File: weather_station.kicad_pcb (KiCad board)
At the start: 2 copper layers, 100 x 140 mm, 78 parts, among them J3 Conn_Coaxial, Q1 Q_NMOS_DGS, U1 LT1129CS8-3.3, U2 ADS1120-PW, U3 nRF52832, U4 LP3947, U5 MPL115A1, U6 MPU-9250, Y1 FL3200037

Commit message: updates
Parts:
- removed D1: D_Zener, Diodes_SMD:D_0603
- added AE1: ant, Microwave:SMA, F.Cu at (93.7, 86.6)
- added C29: C_Small, Capacitors_SMD:C_0402, B.Cu at (61.2, 88.6)
- added C30: C_Small, Capacitors_SMD:C_0402, B.Cu at (61.2, 93.7)
- added J1: Conn_02x10_Odd_Even, Pin_Headers:Pin_Header_Straight_2x10_Pitch2.54mm, F.Cu at (119.0, 172.7)
- added J2: Conn_02x10_Odd_Even, Pin_Headers:Pin_Header_Straight_2x10_Pitch2.54mm, F.Cu at (115.6, 59.9)
- added J4: Conn_Coaxial, Connectors:SMA_SMD_Jack_Straight, B.Cu at (85.9, 76.4)
- added M1: ANEOMETER, Wire_Connections_Bridges:WireConnection_2.00mmDrill, B.Cu at (24.1, 94.5)
- added R21: R_Small, Resistors_SMD:R_0603, B.Cu at (36.6, 94.3)
- added Y2: 32.786khz, Crystals:Crystal_SMD_EuroQuartz_EQ161-2pin_3.2x1.5mm, B.Cu at (61.2, 91.2)
- JP1: moved to B.Cu
- moved C18 60.3 mm to (52.1, 103.1), turned to 270 degrees
- moved L4 18.5 mm to (88.1, 86.4), turned to 270 degrees
- moved D2 18.4 mm to (77.5, 74.4), turned to 270 degrees
- moved C13 16.6 mm to (89.7, 86.3), turned to 90 degrees
- moved C12 16.5 mm to (86.4, 86.1), turned to 270 degrees
- moved L3 15.1 mm to (82.5, 86.4), turned to 90 degrees
- moved R7 13.9 mm to (76.2, 78.5), turned to 90 degrees
- moved R8 13.0 mm to (77.5, 78.5), turned to 90 degrees
- moved R9 12.4 mm to (78.7, 78.5), turned to 90 degrees
- moved C11 12.0 mm to (81.3, 86.4), turned to 270 degrees
- moved C8 7.29 mm to (65.5, 96.1)
- moved C10 6.82 mm to (67.1, 96.0)
- moved C9 1.30 mm to (75.9, 90.7), turned to 0 degrees
- turned JP1 to 90 degrees
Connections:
- U3 pad 10: Net-(U3-Pad10) -> ANEOMETER
- U3 pad 16: RADIO_PTT -> RADIO_PD
- U3 pad 17: RADIO_DATA -> RADIO_PTT
- U3 pad 18: RADIO_UART_TX -> RADIO_DATA
- U3 pad 19: RADIO_UART_RX -> RADIO_UART_TX
- U3 pad 2: Net-(U3-Pad2) -> XL1
- U3 pad 20: Net-(U3-Pad20) -> RADIO_UART_RX
- U3 pad 3: Net-(U3-Pad3) -> XL2
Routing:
- net +3V3: track 150.7 -> 241.2 mm
- net SWDIO: track 0.00 -> 73.5 mm
- net RESET: track 0.00 -> 73.4 mm
- net SWO: track 0.00 -> 71.1 mm
- net RADIO_PD: track 0.00 -> 70.1 mm
- net SWCLK: track 0.00 -> 64.1 mm
- net ANEOMETER: track 0.00 -> 44.7 mm
- net Net-(C12-Pad2): track 0.00 -> 16.8 mm
- net Net-(M1-Pad1): track 0.00 -> 11.8 mm
- net Net-(C11-Pad1): track 0.00 -> 9.93 mm
- net Net-(C11-Pad2): track 0.00 -> 9.64 mm
- net GND: track 62.1 -> 71.4 mm, vias 16 -> 19
- net XL2: track 0.00 -> 7.89 mm
- net XL1: track 0.00 -> 7.55 mm
- net R_LED: track 18.8 -> 11.3 mm
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- added copper zone on F.Cu, net GND

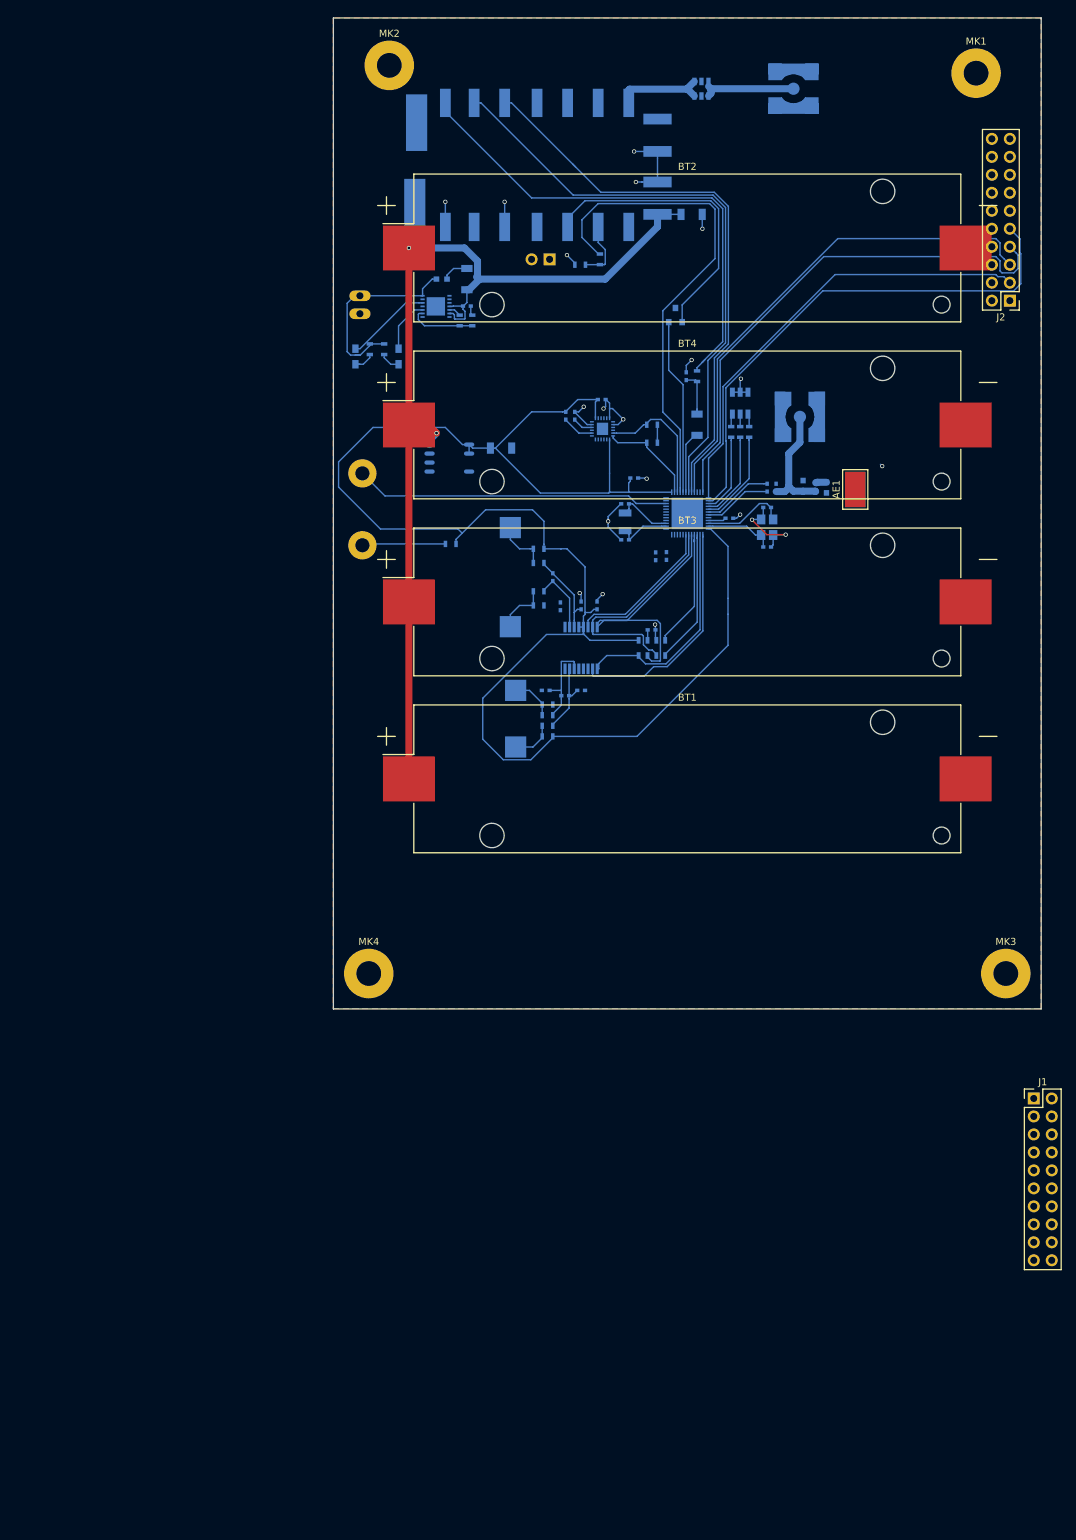
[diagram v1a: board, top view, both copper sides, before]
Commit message: basing solar power supply off of openMPPT
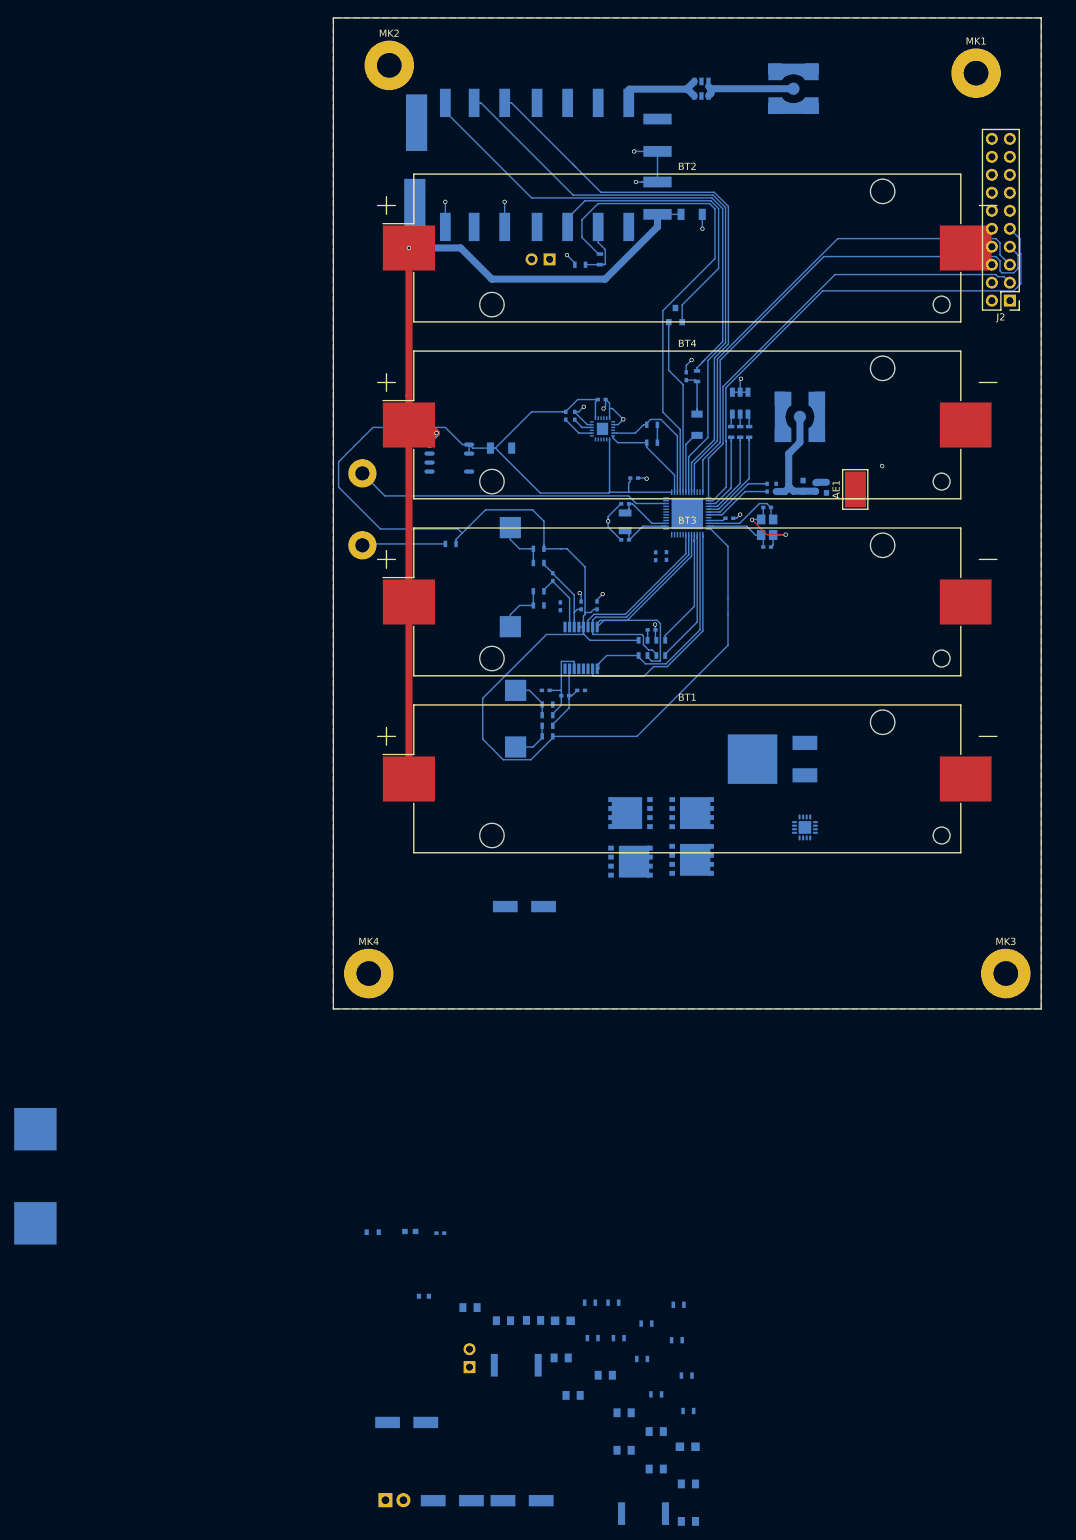
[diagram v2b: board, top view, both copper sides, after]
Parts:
- removed J1: Conn_02x10_Odd_Even, Pin_Headers:Pin_Header_Straight_2x10_Pitch2.54mm
- removed SC1: Solar_Cell, Connectors:PINHEAD1-2
- added C31: 0.1uF, Capacitors_SMD:C_0805, B.Cu at (65.6, 219.7)
- added C32: 1.0uF, Capacitors_SMD:C_0805, B.Cu at (65.6, 225.0)
- added C33: 0.1uF, Capacitors_SMD:C_0805, B.Cu at (70.2, 227.1)
- added C34: 1.0uF, Capacitors_SMD:C_0805, B.Cu at (61.1, 217.1)
- added C35: CP, Capacitors_SMD:CP_Elec_6.3x7.7, B.Cu at (30.4, 218.4)
- added C36: CP, Capacitors_SMD:CP_Elec_6.3x7.7, B.Cu at (47.0, 145.5)
- added C37: 1.0uF, Capacitors_SMD:C_0805, B.Cu at (70.2, 232.4)
- added C38: 0.1uF, Capacitors_SMD:C_0805, B.Cu at (61.1, 222.4)
- added C39: 1.0uF, Capacitors_SMD:C_0805, B.Cu at (39.3, 202.2)
- added C40: CP, Capacitors_SMD:CP_Elec_6.3x7.7, B.Cu at (36.8, 229.5)
- added C41: 0.1uF, Capacitors_SMD:C_0805, B.Cu at (44.0, 204.0)
- added C42: 0.1uF, Capacitors_SMD:C_0805, B.Cu at (53.9, 214.6)
- added C43: CP, Capacitors_SMD:CP_Elec_6.3x7.7, B.Cu at (46.7, 229.5)
- added D1: D_Zener, Diodes_SMD:D_0603, B.Cu at (25.6, 191.5)
- added D5: LED, LEDs:LED_0805, B.Cu at (52.4, 204.1)
- added D6: LED, LEDs:LED_0805, B.Cu at (70.1, 221.9)
- added J5: THERM, Connectors_Terminal_Blocks:TerminalBlock_Pheonix_MPT-2.54mm_2pol, B.Cu at (27.4, 229.4)
- added J6: SOLAR, Pin_Headers:Pin_Header_Straight_1x02_Pitch2.54mm, B.Cu at (39.2, 210.6)
- added L1: 15uH, Capacitors_SMD:C_0402, B.Cu at (35.1, 191.7)
- added L2: 10uH, Capacitors_SMD:C_0603, B.Cu at (30.9, 191.4)
- added L5: 3.3uH, Inductors:Inductor_Wurth_HCI-1890, B.Cu at (-22.1, 183.6)
- added Q2: FDMS8050, TO_SOT_Packages_SMD:TDSON-8-1, B.Cu at (70.6, 132.3)
- added Q3: FDMS8050, TO_SOT_Packages_SMD:TDSON-8-1, B.Cu at (62.0, 132.3)
- added Q4: FDMS8050, TO_SOT_Packages_SMD:TDSON-8-1, B.Cu at (62.0, 139.2)
- added Q5: FDMS8050, TO_SOT_Packages_SMD:TDSON-8-1, B.Cu at (70.6, 138.9)
- added R22: 36k, Resistors_SMD:R_0603, B.Cu at (63.6, 209.5)
- added R23: -, Resistors_SMD:R_0603, B.Cu at (60.3, 206.5)
- added R24: 10, Resistors_SMD:R_0603, B.Cu at (56.3, 201.5)
- added R25: 5.23k, Resistors_SMD:R_0603, B.Cu at (70.2, 216.8)
- added R26: 5.23k, Resistors_SMD:R_0603, B.Cu at (65.6, 214.5)
- added R27: 0.010, Resistors_SMD:R_2512, B.Cu at (63.8, 231.3)
- added R28: 0.010, Resistors_SMD:R_2512, B.Cu at (45.8, 210.3)
- added R29: 499k, Resistors_SMD:R_0603, B.Cu at (56.6, 206.5)
- added R30: 100k, Resistors_SMD:R_0603, B.Cu at (68.5, 206.8)
- C19: value C_Small -> -; footprint Capacitors_SMD:C_0603 -> Capacitors_SMD:C_0805
- C27: value C_Small -> 1.0uF; footprint Capacitors_SMD:C_0402 -> Capacitors_SMD:C_0805
- C28: value C -> 1.0uF; footprint Capacitors_SMD:C_1206 -> Capacitors_SMD:C_0805
- D3: value LED -> MBRD10100CT; footprint LEDs:LED_0603_HandSoldering -> TO_SOT_Packages_SMD:TO-252-2_Rectifier
- D4: value LED -> D_Schottky; footprint LEDs:LED_0603_HandSoldering -> Diodes_SMD:D_SOD-523
- R14: value R_Small -> 10k
- R15: value R_Small -> 5.23k
- R19: value R_Small -> 30.1k
- R20: value R_Small -> 499k
- U4: value LP3947 -> BQ24650; footprint Housings_SON:WSON-14_1EP_4.0x4.0mm_Pitch0.5mm -> Housings_DFN_QFN:QFN-16-1EP_3x3mm_Pitch0.5mm
- moved C28 153.0 mm to (52.2, 209.3), turned to 0 degrees
- moved C27 152.3 mm to (58.4, 211.8)
- moved R20 152.1 mm to (69.9, 211.8), turned to 0 degrees
- moved C19 147.7 mm to (48.3, 204.0), turned to 0 degrees
- moved R15 142.6 mm to (64.2, 204.5), turned to 0 degrees
- moved R19 142.5 mm to (68.8, 201.8), turned to 0 degrees
- moved R14 139.0 mm to (59.6, 201.5), turned to 0 degrees
- moved D4 132.8 mm to (32.8, 200.6), turned to 0 degrees
- moved U4 90.2 mm to (86.6, 134.4), turned to 0 degrees
- moved D3 81.9 mm to (82.0, 124.7), turned to 180 degrees
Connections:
- C19 pad 1: GND -> Net-(C19-Pad1)
- C19 pad 2: Net-(C19-Pad2) -> GND
- C27 pad 1: VCC -> GND
- C28 pad 1: VCC -> /power/VREF
- D3 pad 2: Net-(D3-Pad2) -> Net-(C34-Pad1)
- D4 pad 1: Net-(D4-Pad1) -> Net-(C33-Pad2)
- D4 pad 2: Net-(D4-Pad2) -> Net-(C31-Pad1)
- R14 pad 1: Net-(C19-Pad2) -> Net-(C19-Pad1)
- R14 pad 2: Net-(D3-Pad2) -> GND
- R15 pad 1: Net-(C19-Pad2) -> /power/VREF
- R15 pad 2: Net-(D4-Pad2) -> Net-(C19-Pad1)
- R19 pad 1: Net-(R19-Pad1) -> Net-(C19-Pad1)
- R19 pad 2: Net-(R19-Pad2) -> GND
- R20 pad 1: Net-(C27-Pad2) -> Net-(D3-Pad1)
- R20 pad 2: Net-(R19-Pad1) -> /power/MPPTSET
- U4 pad 1: Net-(U4-Pad1) -> Net-(C27-Pad2)
- U4 pad 10: Net-(D4-Pad1) -> Net-(C38-Pad2)
- U4 pad 12: Net-(D3-Pad1) -> Net-(C31-Pad1)
- U4 pad 13: Net-(U4-Pad13) -> /power/LOW_DRIVE
- U4 pad 14: Net-(C19-Pad2) -> Net-(C33-Pad1)
- U4 pad 15: Net-(U4-Pad15) -> /power/HIGH_DRIVE
- U4 pad 2: SCL -> /power/MPPTSET
- U4 pad 3: SDA -> /power/STAT1
- U4 pad 4: VCC -> Net-(C19-Pad1)
- U4 pad 5: Net-(R19-Pad2) -> /power/STAT2
- U4 pad 6: VCC -> /power/VREF
- U4 pad 7: Net-(U4-Pad7) -> /power/VREF
- U4 pad 9: Net-(R19-Pad1) -> VCC
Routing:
- net Net-(C19-Pad2): track 28.3 -> 0.00 mm
- net VCC: track 139.3 -> 126.5 mm
- net Net-(D3-Pad1): track 12.3 -> 0.00 mm
- net Net-(R19-Pad1): track 9.39 -> 0.00 mm
- net Net-(D4-Pad1): track 7.55 -> 0.00 mm
- net GND: track 71.4 -> 67.6 mm
- net Net-(D3-Pad2): track 3.52 -> 0.00 mm
- net Net-(D4-Pad2): track 3.02 -> 0.00 mm
- net Net-(R19-Pad2): track 1.75 -> 0.00 mm
- net Net-(C27-Pad2): track 1.37 -> 0.00 mm
- added copper zone on B.Cu, net GND

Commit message: well this is going to be easy to route...
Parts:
- removed D1: D_Zener, Diodes_SMD:D_0603
- removed L1: 15uH, Capacitors_SMD:C_0402
- removed L2: 10uH, Capacitors_SMD:C_0603
- moved J5 161.3 mm to (116.5, 95.0), turned to 180 degrees
- moved C28 135.3 mm to (111.0, 87.5), turned to 270 degrees
- moved C19 134.0 mm to (114.5, 87.5), turned to 270 degrees
- moved C38 119.3 mm to (95.0, 108.0)
- moved C32 117.1 mm to (94.5, 111.5)
- moved D6 115.5 mm to (82.0, 107.0), turned to 180 degrees
- moved C42 110.4 mm to (90.5, 110.5), turned to 270 degrees
- moved C33 109.0 mm to (84.0, 119.0), turned to 270 degrees
- moved C31 108.1 mm to (94.5, 115.5)
- moved C37 107.5 mm to (93.5, 127.5), turned to 90 degrees
- moved R26 107.2 mm to (85.0, 109.0), turned to 270 degrees
- moved R30 103.1 mm to (85.0, 105.0), turned to 270 degrees
- moved R15 100.6 mm to (89.0, 107.0), turned to 270 degrees
- moved J6 99.1 mm to (113.3, 144.8)
- moved C27 97.4 mm to (76.0, 116.0)
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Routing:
- net Net-(C33-Pad1): track 0.00 -> 76.4 mm, vias 0 -> 2
- net Net-(C34-Pad1): track 0.00 -> 70.2 mm
- net /power/HIGH_DRIVE: track 0.00 -> 48.4 mm, vias 0 -> 2
- net /power/LOW_DRIVE: track 0.00 -> 34.9 mm, vias 0 -> 3
- net GND: track 67.6 -> 94.2 mm, vias 19 -> 25
- net Net-(C38-Pad2): track 0.00 -> 26.0 mm
- net Net-(D3-Pad1): track 0.00 -> 19.3 mm
- net Net-(C31-Pad1): track 0.00 -> 13.4 mm
- net VCC: track 126.5 -> 139.6 mm
- net Net-(C27-Pad2): track 0.00 -> 8.63 mm
- net Net-(C33-Pad2): track 0.00 -> 3.93 mm
- net +3V3: track 241.2 -> 237.6 mm

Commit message: almost done
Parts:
- moved R25 42.2 mm to (87.1, 104.7)
- moved R29 37.8 mm to (55.0, 123.5)
- moved C39 34.8 mm to (55.0, 129.5)
- moved C42 34.4 mm to (60.0, 126.5), turned to 180 degrees
- moved C41 32.9 mm to (55.0, 126.5)
- moved R30 31.1 mm to (60.0, 123.5), turned to 0 degrees
- moved R15 29.1 mm to (110.5, 87.5), turned to 90 degrees
- moved R24 21.0 mm to (76.8, 120.2)
- moved R23 18.0 mm to (82.0, 120.2)
- moved C37 15.0 mm to (80.4, 120.2)
- moved D5 14.5 mm to (87.1, 100.2)
- moved C34 14.1 mm to (78.4, 120.2)
- moved C32 7.81 mm to (93.5, 119.2)
- moved D6 7.46 mm to (85.1, 100.2), turned to 270 degrees
- moved C31 6.08 mm to (93.5, 121.5)
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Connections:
- J2 pad 10: Net-(J2-Pad10) -> GND
- J2 pad 12: Net-(J2-Pad12) -> GND
- J2 pad 14: Net-(J2-Pad14) -> GND
- J2 pad 16: Net-(J2-Pad16) -> GND
- J2 pad 18: Net-(J2-Pad18) -> GND
- J2 pad 2: Net-(J2-Pad2) -> GND
- J2 pad 20: Net-(J2-Pad20) -> GND
- J2 pad 4: Net-(J2-Pad4) -> GND
- J2 pad 6: Net-(J2-Pad6) -> GND
- J2 pad 8: Net-(J2-Pad8) -> GND
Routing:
- net VCC: track 139.6 -> 220.3 mm, vias 2 -> 4
- net Net-(C38-Pad2): track 26.0 -> 100.3 mm, vias 0 -> 2
- net Net-(C19-Pad1): track 0.00 -> 62.9 mm, vias 0 -> 2
- net Net-(C41-Pad1): track 0.00 -> 48.5 mm, vias 0 -> 2
- net /power/VREF: track 0.00 -> 46.0 mm
- net /power/MPPTSET: track 0.00 -> 43.5 mm, vias 0 -> 2
- net GND: track 94.2 -> 128.9 mm, vias 25 -> 33
- net /power/STAT1: track 0.00 -> 25.0 mm
- net /power/STAT2: track 0.00 -> 16.3 mm
- net Net-(C34-Pad1): track 70.2 -> 83.3 mm
- net Net-(D3-Pad1): track 19.3 -> 24.9 mm
- net Net-(C27-Pad2): track 8.63 -> 13.5 mm
- net Net-(C33-Pad1): track 76.4 -> 80.4 mm, vias 2 -> 3
- net Net-(C33-Pad2): track 3.93 -> 7.16 mm
- net Net-(D6-Pad2): track 0.00 -> 2.65 mm
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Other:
- net class Default: clearance 0.2 -> 0.1524
- net class big: clearance 0.2 -> 0.1524
- net class radio: clearance 0.2 -> 0.1524
- rule trace_clearance: 0.2 -> 0.1524
- rule trace_min: 0.2 -> 0.1524
- rule via_min_size: 0.4 -> 0.254

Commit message: well that wasn't centered
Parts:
- moved MK1 5.05 mm to (115.0, 25.0)
- moved MK2 3.36 mm to (25.0, 25.0)
- moved C10 1.78 mm to (65.3, 96.0)
- moved C8 1.52 mm to (67.1, 96.1)
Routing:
- net +3V3: track 237.6 -> 321.6 mm
- net Net-(C34-Pad1): track 83.3 -> 123.5 mm
- net GND: track 128.9 -> 157.2 mm, vias 33 -> 59
- net Net-(DRA1-Pad7): track 1.24 -> 18.0 mm
- net VCC: track 220.3 -> 236.3 mm, vias 4 -> 7
- net Net-(C38-Pad2): track 100.3 -> 109.2 mm
- net Net-(C10-Pad2): track 0.00 -> 4.15 mm
- net Net-(C8-Pad1): track 0.00 -> 2.98 mm
- added copper zone on B.Cu, net Net-(C33-Pad1)
- added copper zone on B.Cu, net VCC
